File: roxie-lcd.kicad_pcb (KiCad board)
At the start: 2 copper layers, 25 parts, among them J1 JTAG, J2 LCD_SPI, J3 VESC, U1 AMS1117-3.3, U2 STM32F103C8T6, Y1 8MHz

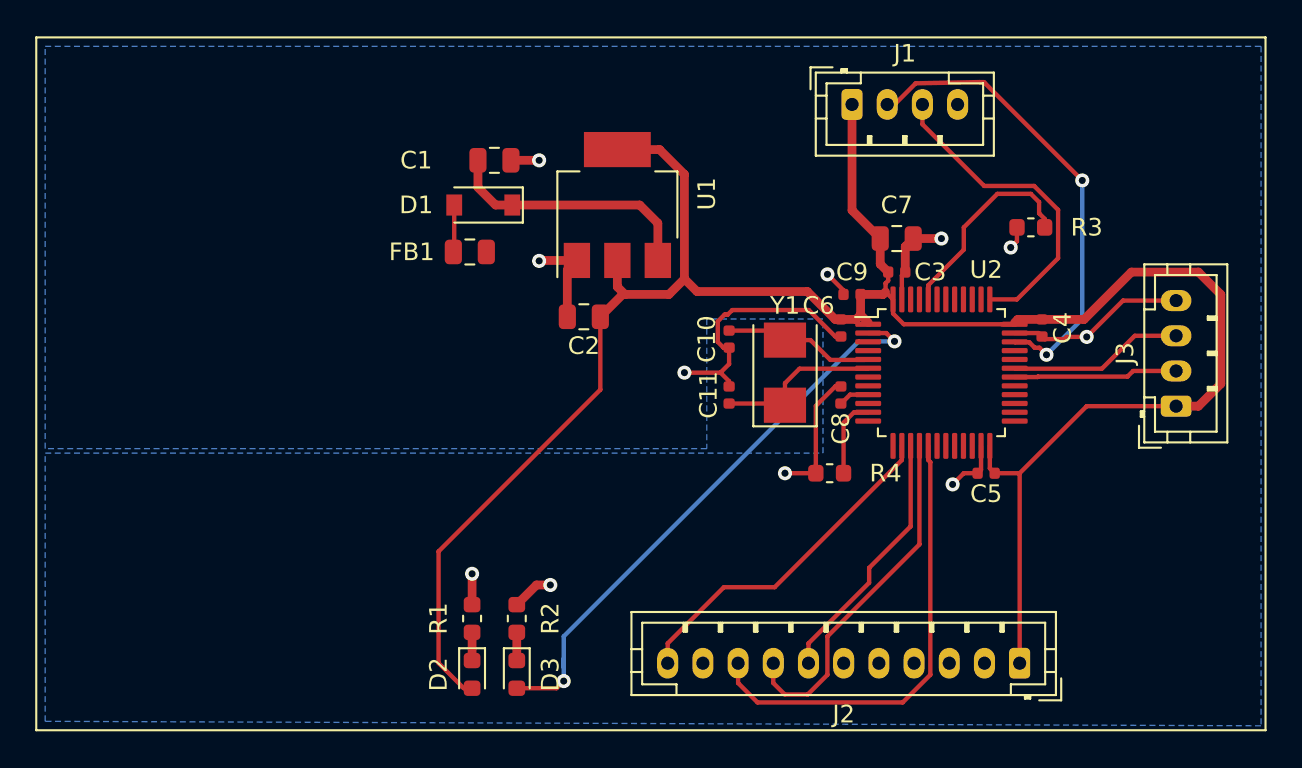
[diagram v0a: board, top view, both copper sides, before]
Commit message: Change connectors
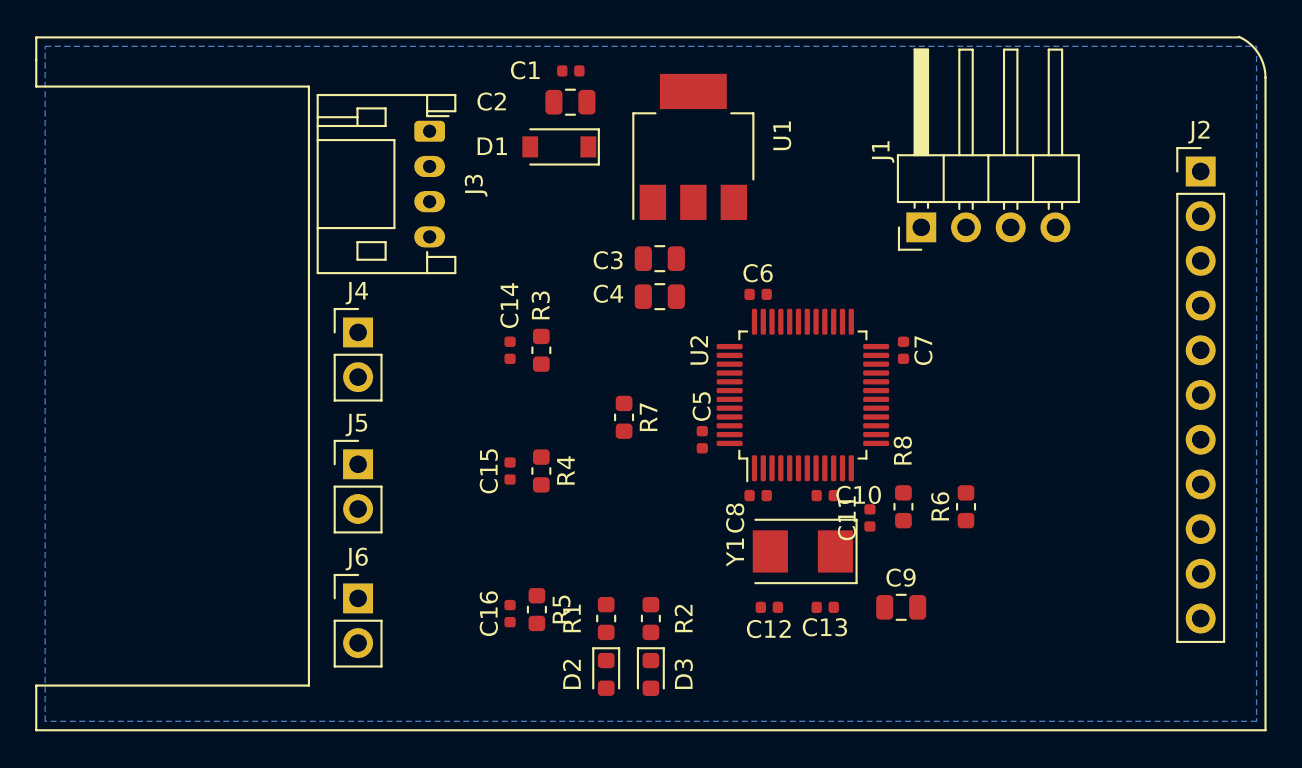
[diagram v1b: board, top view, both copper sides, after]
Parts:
- removed the C7 at (67.9, 30.5)
- removed FB1: Ferrite_Bead_Small, Inductor_SMD:L_0805_2012Metric
- added C1: 100n, Capacitor_SMD:C_0402_1005Metric, F.Cu at (49.4, 21.0)
- added C14: 100n, Capacitor_SMD:C_0402_1005Metric, F.Cu at (46.0, 36.8)
- added C15: 100n, Capacitor_SMD:C_0402_1005Metric, F.Cu at (46.0, 43.7)
- added C16: 100n, Capacitor_SMD:C_0402_1005Metric, F.Cu at (46.0, 51.8)
- added C4: 22u, Capacitor_SMD:C_0805_2012Metric, F.Cu at (54.5, 33.8)
- added C9: 10u, Capacitor_SMD:C_0805_2012Metric, F.Cu at (68.2, 51.4)
- added J4: UP, Connector_PinHeader_2.54mm:PinHeader_1x02_P2.54mm_Vertical, F.Cu at (37.3, 35.8)
- added J5: DOWN, Connector_PinHeader_2.54mm:PinHeader_1x02_P2.54mm_Vertical, F.Cu at (37.3, 43.3)
- added J6: SELECT, Connector_PinHeader_2.54mm:PinHeader_1x02_P2.54mm_Vertical, F.Cu at (37.3, 50.9)
- added R4: 10k, Resistor_SMD:R_0603_1608Metric, F.Cu at (47.8, 43.7)
- added R5: 10k, Resistor_SMD:R_0603_1608Metric, F.Cu at (47.5, 51.6)
- added R6: 10k, Resistor_SMD:R_0603_1608Metric, F.Cu at (71.9, 45.7)
- added R7: 10k, Resistor_SMD:R_0603_1608Metric, F.Cu at (52.5, 40.6)
- C12: renamed from C10; value 20p -> 15p
- C13: renamed from C11; value 20p -> 15p
- C3: renamed from C2; value 10u -> 22u
- J1: footprint Connector_JST:JST_PH_B4B-PH-K_1x04_P2.00mm_Vertical -> Connector_PinHeader_2.54mm:PinHeader_1x04_P2.54mm_Horizontal
- J2: footprint Connector_JST:JST_PH_B11B-PH-K_1x11_P2.00mm_Vertical -> Connector_PinHeader_2.54mm:PinHeader_1x11_P2.54mm_Vertical
- J3: footprint Connector_JST:JST_PH_B4B-PH-K_1x04_P2.00mm_Vertical -> Connector_JST:JST_PH_S4B-PH-K_1x04_P2.00mm_Horizontal
- moved J3 45.2 mm to (41.4, 24.4), turned to 270 degrees
- moved J2 29.8 mm to (85.2, 26.7), turned to 0 degrees
- moved R3 28.7 mm to (47.8, 36.8), turned to 270 degrees
- moved C6 16.2 mm to (60.1, 33.7), turned to 0 degrees
- moved C12 15.4 mm to (60.7, 51.4), turned to 0 degrees
- moved C5 14.6 mm to (56.9, 41.9), turned to 90 degrees
- moved C13 13.2 mm to (63.9, 51.4), turned to 180 degrees
- moved C11 12.7 mm to (66.4, 46.4), turned to 270 degrees
- moved C8 10.6 mm to (60.1, 45.1), turned to 0 degrees
- moved Y1 10.2 mm to (62.6, 48.3), turned to 180 degrees
- moved C7 8.42 mm to (68.3, 36.8), turned to 270 degrees
- moved J1 8.02 mm to (69.3, 29.8), turned to 90 degrees
- moved U2 7.98 mm to (62.6, 39.4), turned to 90 degrees
- moved D2 7.62 mm to (51.4, 55.2)
- moved D3 7.62 mm to (54.0, 55.2)
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- renumbered C8 to C10, C9 to C11, C1 to C2, C3 to C5, C4 to C6, C5 to C7, C6 to C8, R4 to R8
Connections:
- net CANRX renamed CAN_RX
- D1 pad 2: Net-(D1-Pad2) -> VCC
- J3 pad 1: +3.3VA -> VCC
- R3 pad 1: BOOT0 -> +3.3VA
- R3 pad 2: GND -> BTN_UP
- U2 pad 39: Net-(U2-Pad39) -> BTN_UP
- U2 pad 40: Net-(U2-Pad40) -> BTN_DOWN
- U2 pad 41: Net-(U2-Pad41) -> BTN_SELECT
- U2 pad 7: NRST -> Net-(R6-Pad2)
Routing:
- net +3.3VA: track 126.2 -> 0.00 mm
- net GND: track 54.9 -> 0.00 mm, vias 11 -> 0
- net Net-(D3-Pad2): track 33.3 -> 0.00 mm, vias 2 -> 0
- net SWDIO: track 27.1 -> 0.00 mm, vias 2 -> 0
- net MOSI: track 26.2 -> 0.00 mm
- net MISO: track 20.1 -> 0.00 mm
- net SS: track 19.5 -> 0.00 mm
- net SWCLK: track 18.4 -> 0.00 mm
- net SCK: track 14.8 -> 0.00 mm
- net Net-(C1-Pad1): track 14.7 -> 0.00 mm
- net BOOT0: track 11.8 -> 0.00 mm
- net UART_RX: track 9.96 -> 0.00 mm
- net HSE_OUT: track 9.54 -> 0.00 mm
- net UART_TX: track 9.32 -> 0.00 mm
- net HSE_IN: track 8.60 -> 0.00 mm
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
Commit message: Quick pcb routing
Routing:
- net +3.3VA: track 0.00 -> 96.2 mm
- net GND: track 0.00 -> 69.1 mm, vias 0 -> 17
- net BTN_SELECT: track 0.00 -> 33.1 mm
- net UART_TX: track 0.00 -> 27.1 mm, vias 0 -> 1
- net BTN_DOWN: track 0.00 -> 26.3 mm
- net UART_RX: track 0.00 -> 25.3 mm, vias 0 -> 1
- net SWDIO: track 0.00 -> 22.9 mm, vias 0 -> 1
- net SS: track 0.00 -> 22.8 mm
- net BTN_UP: track 0.00 -> 21.9 mm
- net SWCLK: track 0.00 -> 21.4 mm, vias 0 -> 2
- net MOSI: track 0.00 -> 21.4 mm, vias 0 -> 1
- net MISO: track 0.00 -> 20.2 mm, vias 0 -> 1
- net SCK: track 0.00 -> 18.8 mm
- net Net-(D3-Pad2): track 0.00 -> 18.0 mm, vias 0 -> 2
- net Net-(C1-Pad1): track 0.00 -> 15.8 mm
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- added copper zone on F.Cu, net +3.3VA
